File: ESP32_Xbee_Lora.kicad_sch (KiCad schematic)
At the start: 0 parts

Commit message: Power Supply Schematic Completed
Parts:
- added C1: 1000uF, LOGSUN:LGS-KC-140CLH-1010, symbol LOGSUN:LGS-KC-SMD&DIP
- added C2, C3: 0.1uF, symbol Device:C_Small
- added C4: 1uF, symbol Device:C_Small
- added C5: 100uF, symbol Device:C_Polarized_Small
- added D1: W10G, Diode_THT:Diode_Bridge_Round_D9.8mm, symbol Diode_Bridge:W10G
- added D2: 1N5822, Diode_THT:D_DO-201AD_P15.24mm_Horizontal, symbol Diode:1N5822
- added D3: RED, symbol Device:LED_Small
- added D4: 1N5819, Diode_THT:D_DO-41_SOD81_P10.16mm_Horizontal, symbol Diode:1N5819
- added J1: ~, LOGSUN:LGS-KC-VALCON_CSP-USC16-TR, symbol LOGSUN:LGS-KC-CSP-USC16-TR
- added J2: Barrel_Jack_Switch, symbol Connector:Barrel_Jack_Switch
- added L1: 220uH, LOGSUN:LGS-KC-MS42, symbol LOGSUN:LGS-KC-DIL4
- added Q1: AO3401A, Package_TO_SOT_SMD:SOT-23, symbol Transistor_FET:AO3401A
- added R1: 10K, symbol Device:R_Small
- added R2: 1K, symbol Device:R_Small
- added S1: Tact_SW, LOGSUN:LGS-KC-B3F-10XX, symbol LOGSUN:LGS-KC-10-XX
- added SW1: Power_SW, LOGSUN:LGS-KC-SLIDE, symbol LOGSUN:LGS-KC-SW
- added U1: ~, nitin:esp 32 wroom module, symbol NITIN:esp32_wroom_module
- added U2: LM2576S-5, Package_TO_SOT_SMD:TO-263-5_TabPin3, symbol Regulator_Switching:LM2576S-5
- added U3: LM1117MP-3.3, Package_TO_SOT_SMD:SOT-223-3_TabPin2, symbol Regulator_Linear:LM1117MP-3.3
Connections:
- new net: D2.1 (K), L1.1, L1.P1 (2), U2.2 (OUT)
- new net: C1.P1, C1.S1 (P2), D4.2 (A), L1.2 (3), L1.P2 (4), Q1.1 (G), R1.1
- new net: D3.1 (K), R2.1
- new net: J1.A1 (GND_A), J1.A12 (GND_A)
- new net: J1.A4 (VBUS_A), J1.A9 (VBUS_A)
- new net: J1.B1 (GND_B), J1.B12 (GND_B)
- new net: J1.B4 (VBUS_B), J1.B9 (VBUS_B)
- new net: J1.S1 (SHELL_GND), J1.S2 (SHELL_GND), J1.S3 (SHELL_GND), J1.S4 (SHELL_GND)
- new net +12P: D1.4, J2.1
- new net +12V: C5.1, SW1.5, SW1.6, U2.1 (VIN)
- new net +12_{EXT}: D1.1 (+), SW1.3, SW1.4
- new net +3.3V: C3.1, C4.1, D3.2 (A), U3.2 (VO)
- new net +5V: C2.1, D4.1 (K), Q1.2 (S), U3.3 (VI)
- new net GND: C1.P2 (P3), C1.S2 (P4), C2.2, C3.2, C4.2, C5.2, D1.3 (-), D2.2 (A), R1.2, R2.2, U2.3 (GND), U2.5 (~{ON}/OFF), U3.1 (GND)
- new net GNDPWR: D1.2, J2.2
- new net V_{USB}: Q1.3 (D)
- no-connect marks 0 -> 2
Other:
- note added: "Power Supply"

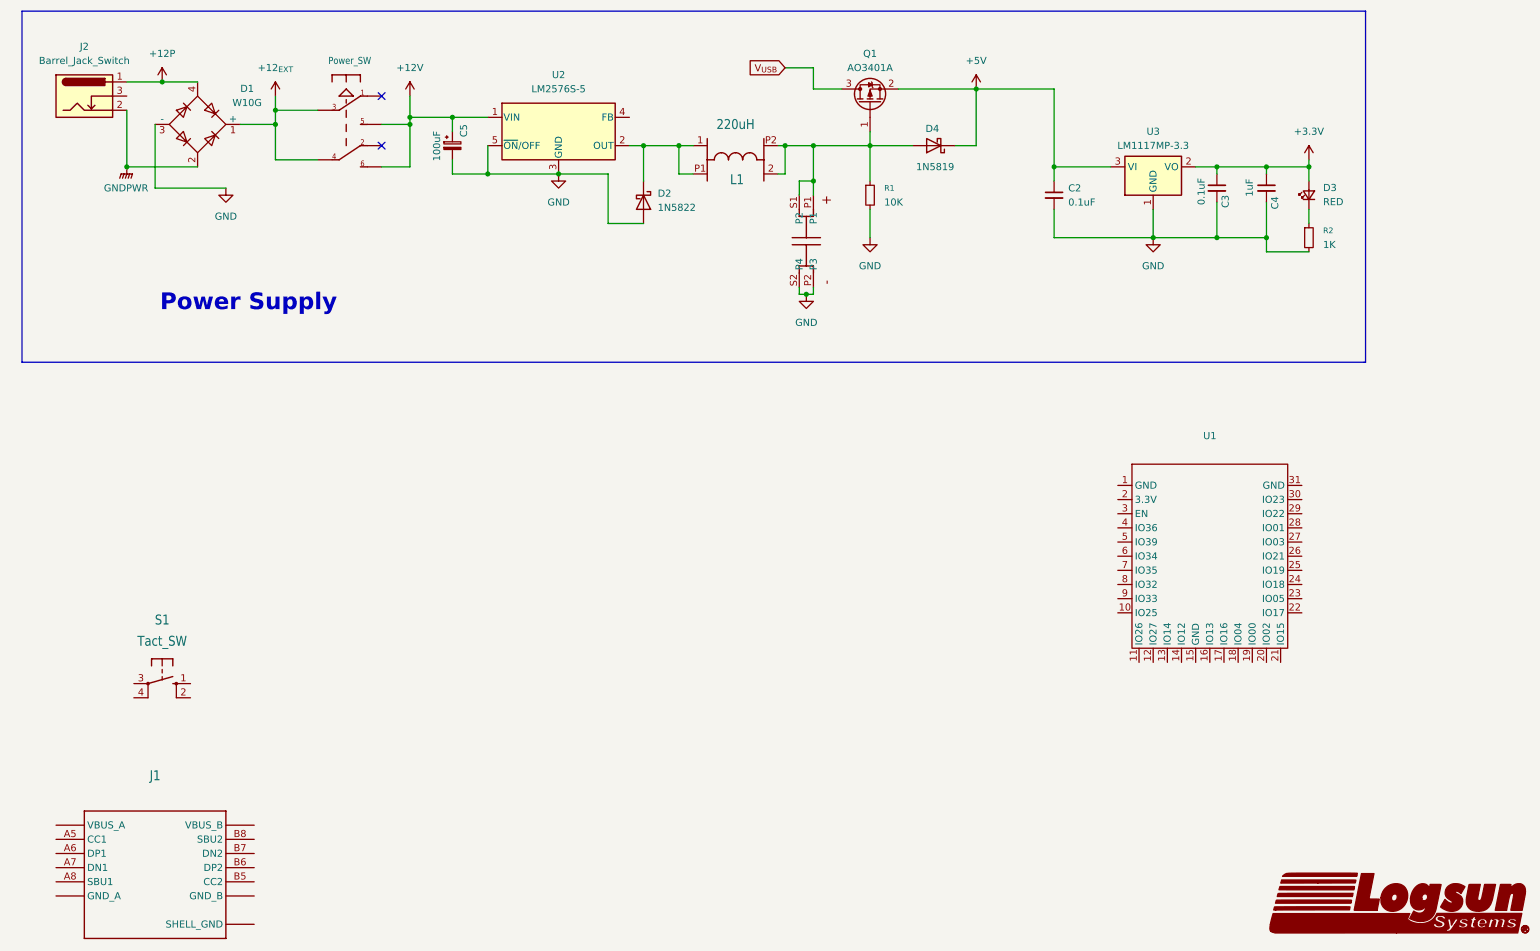
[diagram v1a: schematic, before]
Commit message: Controller Section Schematic Done
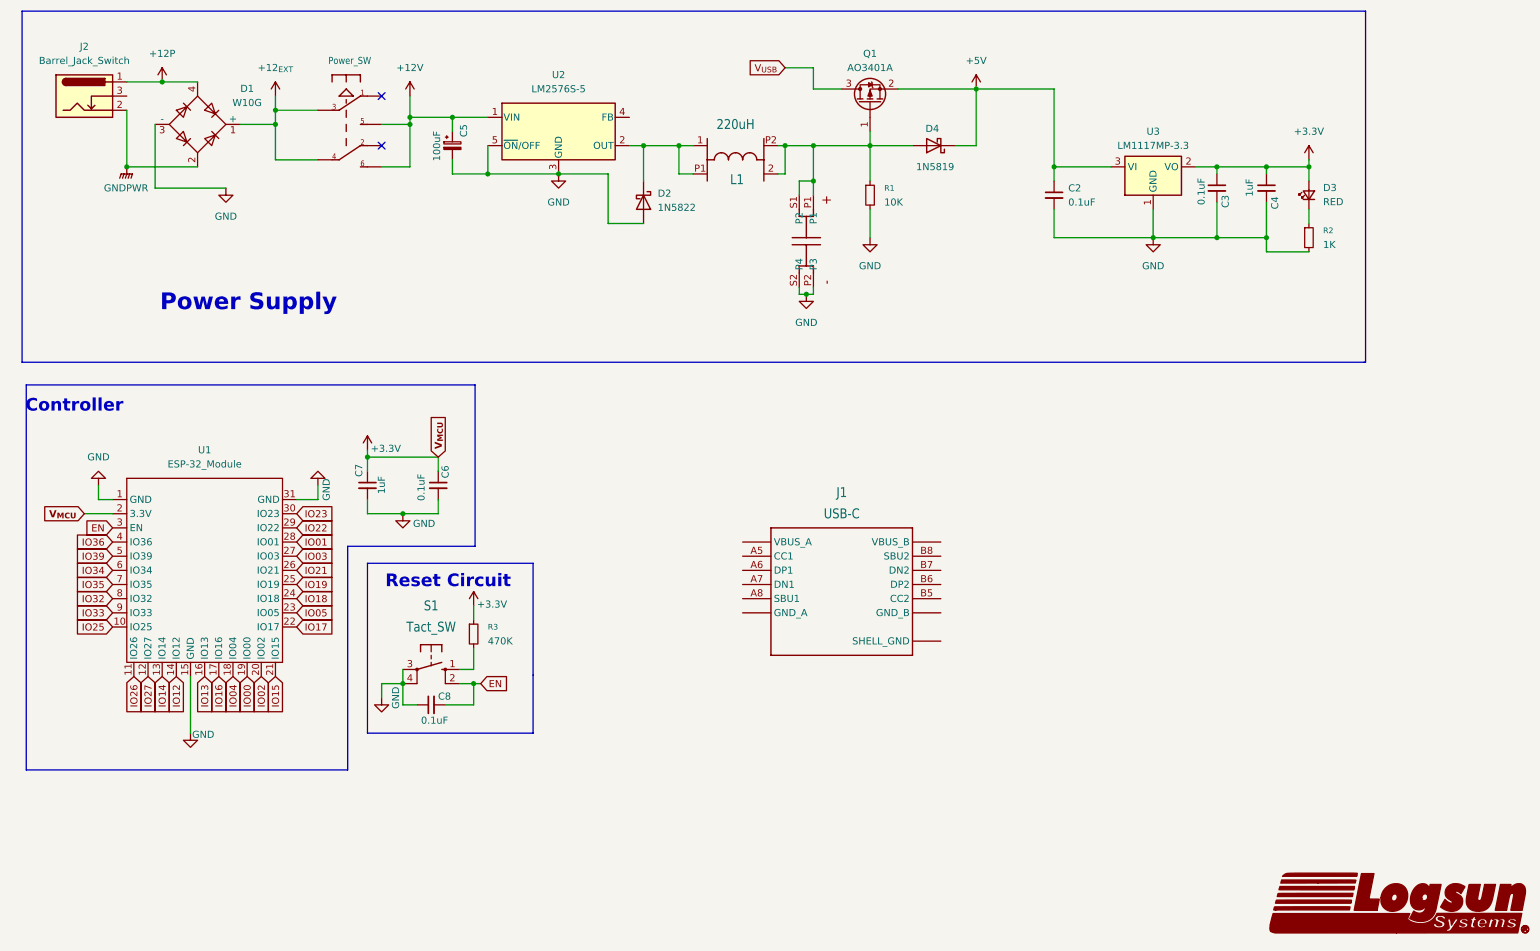
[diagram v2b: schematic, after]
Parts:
- added C6, C8: 0.1uF, symbol Device:C_Small
- added C7: 1uF, symbol Device:C_Small
- added R3: 470K, symbol Device:R_Small
- J1: value ~ -> USB-C
- U1: value ~ -> ESP-32_Module
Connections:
- net +3.3V: now also U1.2 (3.3V), C6.1, C7.1, R3.1
- net GND: now also S1.3 (P), S1.4 (P1), U1.1 (GND), U1.15 (GND), U1.31 (GND), C6.2, C7.2, C8.1
- net IO25: now reaches U1.10 (IO25)
- net IO26: now reaches U1.11 (IO26)
- net IO27: now reaches U1.12 (IO27)
- net IO14: now reaches U1.13 (IO14)
- net IO12: now reaches U1.14 (IO12)
- net IO13: now reaches U1.16 (IO13)
- net IO16: now reaches U1.17 (IO16)
- net IO04: now reaches U1.18 (IO04)
- net IO00: now reaches U1.19 (IO00)
- net IO02: now reaches U1.20 (IO02)
- net IO15: now reaches U1.21 (IO15)
- net IO17: now reaches U1.22 (IO17)
- net IO05: now reaches U1.23 (IO05)
- net IO18: now reaches U1.24 (IO18)
- net IO19: now reaches U1.25 (IO19)
- net IO21: now reaches U1.26 (IO21)
- net IO03: now reaches U1.27 (IO03)
- net IO01: now reaches U1.28 (IO01)
- net IO22: now reaches U1.29 (IO22)
- net EN: now reaches U1.3 (EN)
- net EN: now also S1.2 (S1), C8.2
- net IO23: now reaches U1.30 (IO23)
- net IO36: now reaches U1.4 (IO36)
- net IO39: now reaches U1.5 (IO39)
- net IO34: now reaches U1.6 (IO34)
- net IO35: now reaches U1.7 (IO35)
- net IO32: now reaches U1.8 (IO32)
- net IO33: now reaches U1.9 (IO33)
- net at S1.1 (S): now also R3.2
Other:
- note added: "Controller"
- note added: "Reset Circuit"
- moved on the sheet: J1, S1, U1

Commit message: LED Switch secton done and schematic files added for other sections
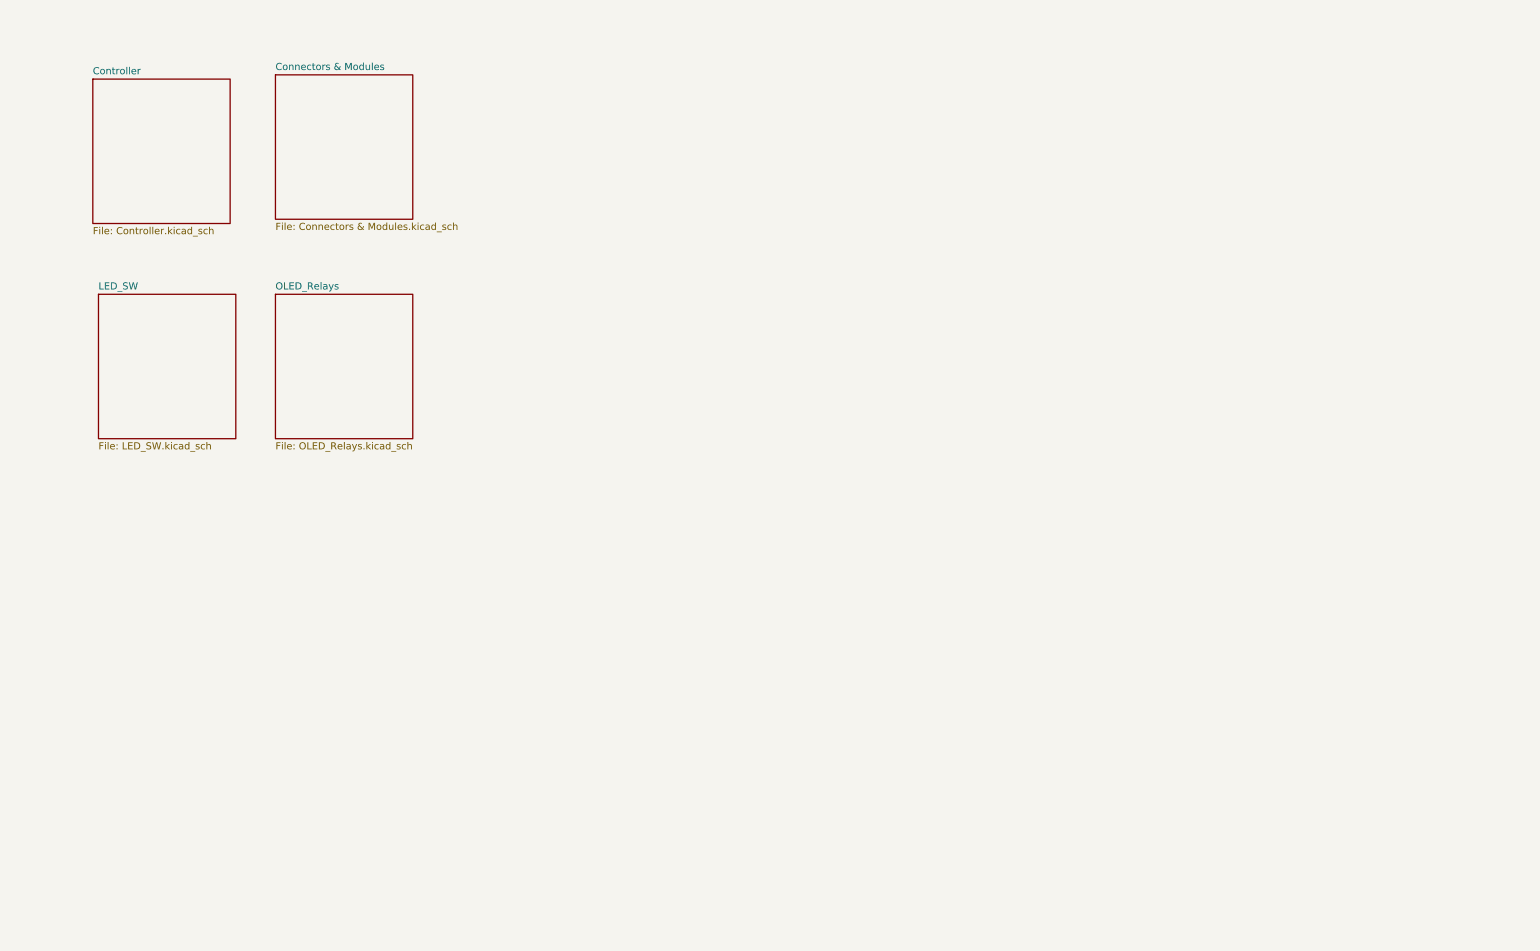
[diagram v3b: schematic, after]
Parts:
- removed C1: 1000uF, LOGSUN:LGS-KC-140CLH-1010, symbol LOGSUN:LGS-KC-SMD&DIP
- removed C2, C3, C6, C8: 0.1uF, symbol Device:C_Small
- removed C4, C7: 1uF, symbol Device:C_Small
- removed C5: 100uF, symbol Device:C_Polarized_Small
- removed D1: W10G, Diode_THT:Diode_Bridge_Round_D9.8mm, symbol Diode_Bridge:W10G
- removed D2: 1N5822, Diode_THT:D_DO-201AD_P15.24mm_Horizontal, symbol Diode:1N5822
- removed D3: RED, symbol Device:LED_Small
- removed D4: 1N5819, Diode_THT:D_DO-41_SOD81_P10.16mm_Horizontal, symbol Diode:1N5819
- removed J1: USB-C, LOGSUN:LGS-KC-VALCON_CSP-USC16-TR, symbol LOGSUN:LGS-KC-CSP-USC16-TR
- removed J2: Barrel_Jack_Switch, symbol Connector:Barrel_Jack_Switch
- removed L1: 220uH, LOGSUN:LGS-KC-MS42, symbol LOGSUN:LGS-KC-DIL4
- removed Q1: AO3401A, Package_TO_SOT_SMD:SOT-23, symbol Transistor_FET:AO3401A
- removed R1: 10K, symbol Device:R_Small
- removed R2: 1K, symbol Device:R_Small
- removed R3: 470K, symbol Device:R_Small
- removed S1: Tact_SW, LOGSUN:LGS-KC-B3F-10XX, symbol LOGSUN:LGS-KC-10-XX
- removed SW1: Power_SW, LOGSUN:LGS-KC-SLIDE, symbol LOGSUN:LGS-KC-SW
- removed U1: ESP-32_Module, nitin:esp 32 wroom module, symbol NITIN:esp32_wroom_module
- removed U2: LM2576S-5, Package_TO_SOT_SMD:TO-263-5_TabPin3, symbol Regulator_Switching:LM2576S-5
- removed U3: LM1117MP-3.3, Package_TO_SOT_SMD:SOT-223-3_TabPin2, symbol Regulator_Linear:LM1117MP-3.3
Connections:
- no-connect marks 2 -> 0
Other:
- added sheet Connectors & Modules (Connectors & Modules.kicad_sch)
- added sheet Controller (Controller.kicad_sch)
- added sheet LED_SW (LED_SW.kicad_sch)
- added sheet OLED_Relays (OLED_Relays.kicad_sch)
- note removed: "Controller"
- note removed: "Power Supply"
- note removed: "Reset Circuit"

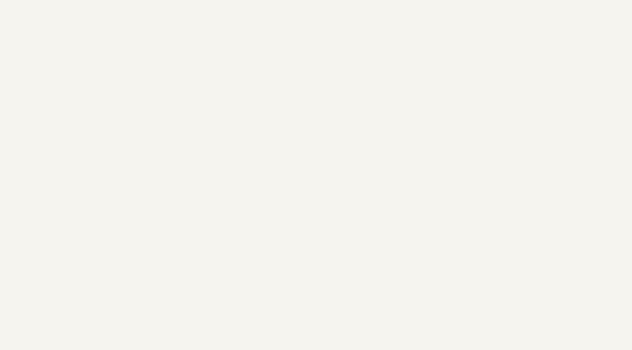
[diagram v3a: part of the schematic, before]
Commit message: OLED, Relay and Bar graph added
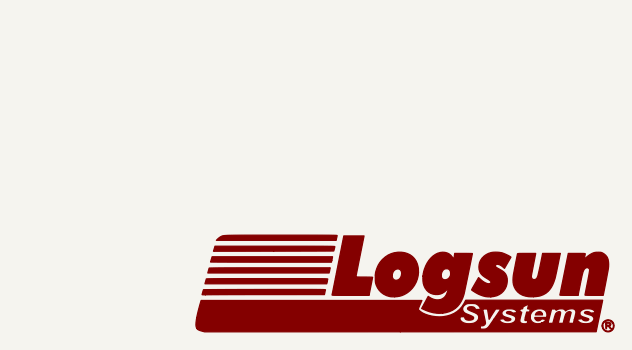
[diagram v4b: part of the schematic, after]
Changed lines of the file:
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@@
 		(company "Logsun Systems")
+	)
+	(symbol
+		(lib_id "Logsun_Logo:LOGO")
+		(at 255.27 173.99 0)
+		(unit 1)
+		(exclude_from_sim no)
+		(in_bom yes)
+		(on_board yes)
+		(dnp no)
+		(fields_autoplaced yes)
+		(property "Reference" "#G2"
+			(at 255.27 168.025 0)
+			(effects
+				(font
+					(size 1.27 1.27)
+				)
+				(hide yes)
+			)
+		)
+		(property "Value" "LOGO"
+			(at 255.27 179.955 0)
+			(effects
+				(font
+					(size 1.27 1.27)
+				)
+				(hide yes)
+			)
+		)
+		(property "Footprint" ""
+			(at 255.27 173.99 0)
+			(effects
+				(font
+					(size 1.27 1.27)
+				)
+				(hide yes)
+			)
+		)
+		(property "Datasheet" ""
+			(at 255.27 173.99 0)
+			(effects
+				(font
+					(size 1.27 1.27)
+				)
+				(hide yes)
+			)
+		)
+		(property "Description" ""
+			(at 255.27 173.99 0)
+			(effects
+				(font
+					(size 1.27 1.27)
+				)
+				(hide yes)
+			)
+		)
+		(instances
+			(project "ESP32_Xbee_Lora"
+				(path "/99e6c4b3-8320-4218-aa5a-41657e7e07c6"
+					(reference "#G2")
+					(unit 1)
+				)
+			)
+		)
 	)
 	(sheet

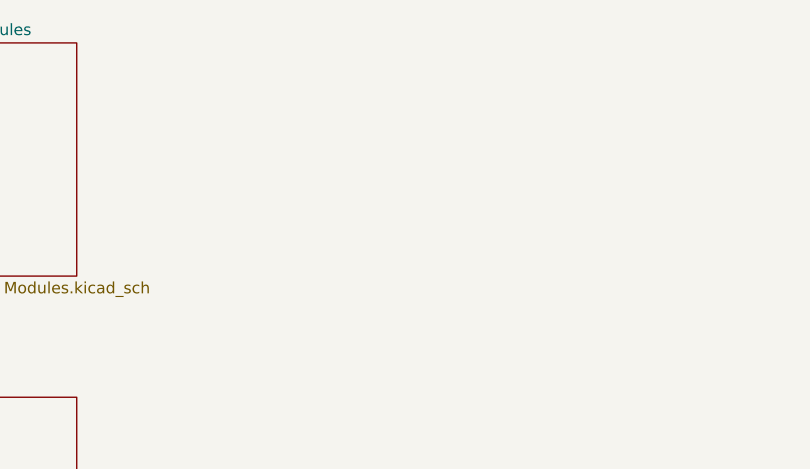
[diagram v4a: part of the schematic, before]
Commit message: RGB,POT and sensors added
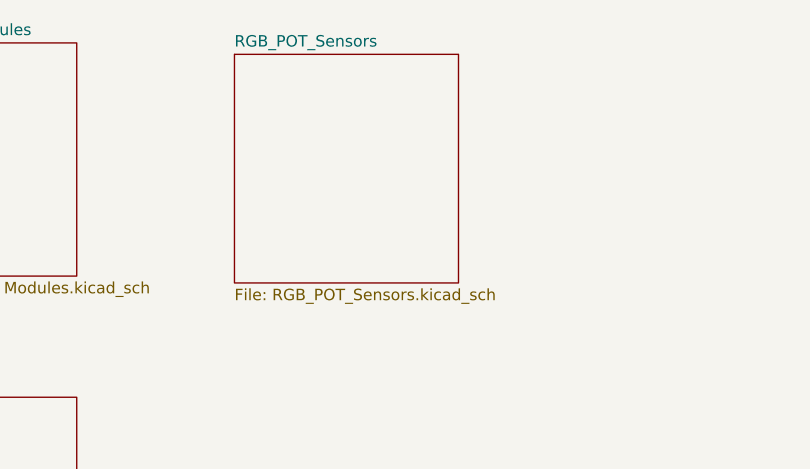
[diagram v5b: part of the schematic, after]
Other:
- added sheet RGB_POT_Sensors (RGB_POT_Sensors.kicad_sch)
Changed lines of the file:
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@@
+		)
+	)
+	(sheet
+		(at 101.854 25.4)
+		(size 24.892 25.4)
+		(exclude_from_sim no)
+		(in_bom yes)
+		(on_board yes)
+		(dnp no)
+		(fields_autoplaced yes)
+		(stroke
+			(width 0.1524)
+			(type solid)
+		)
+		(fill
+			(color 0 0 0 0.0000)
+		)
+		(property "Sheetname" "RGB_POT_Sensors"
+			(at 101.854 24.6884 0)
+			(effects
+				(font
+					(size 1.27 1.27)
+				)
+				(justify left bottom)
+			)
+		)
+		(property "Sheetfile" "RGB_POT_Sensors.kicad_sch"
+			(at 101.854 51.3846 0)
+			(effects
+				(font
+					(size 1.27 1.27)
+				)
+				(justify left top)
+			)
+		)
+		(instances
+			(project "ESP32_Xbee_Lora"
+				(path "/99e6c4b3-8320-4218-aa5a-41657e7e07c6"
+					(page "6")
+				)
+			)
 		)
 	)
